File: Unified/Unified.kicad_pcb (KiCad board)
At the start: 2 copper layers, 72.4 x 72.4 mm, 56 parts, among them J1 USB_C_Receptacle_USB2.0_16P, J10 JST_switch_1, J11 JST_switch_2, J12 Conn_touch_1, J13 Conn_touch_2, J14 Bat_pos_sel, J15 Bat_neg_sel, J16 JST_header, J2 JST_battery, J3 JST_header, J4 JST_speaker, J5 JST_debug_swd, J6 JST_debug_serial, J7 Conn_speaker_sd, J8 Conn_speaker_gain, J9 Conn_speaker_gnd, Q1 AO3401A, Q2 AO3400A, SW1 SW_power, U1 MCP73831-2-OT, U2 MAX98357A

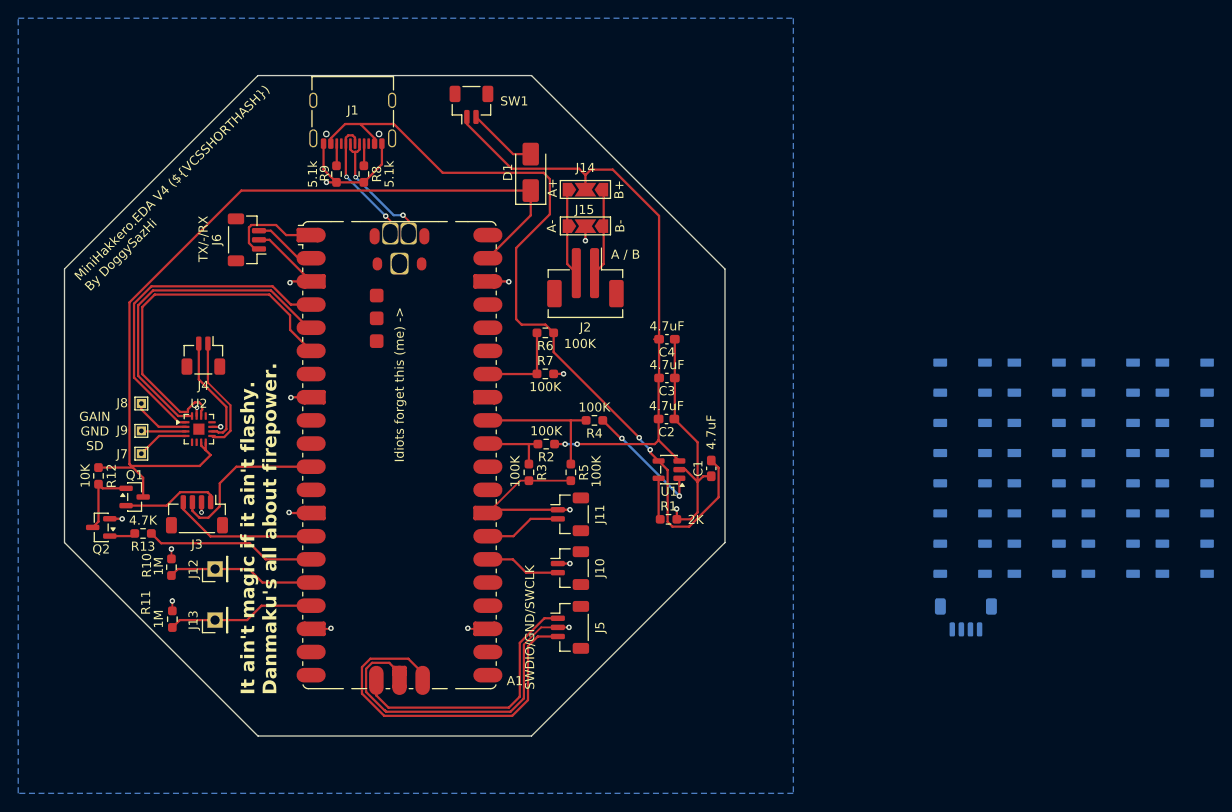
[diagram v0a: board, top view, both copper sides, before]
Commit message: Add LEDs to unified PCB, currently routing
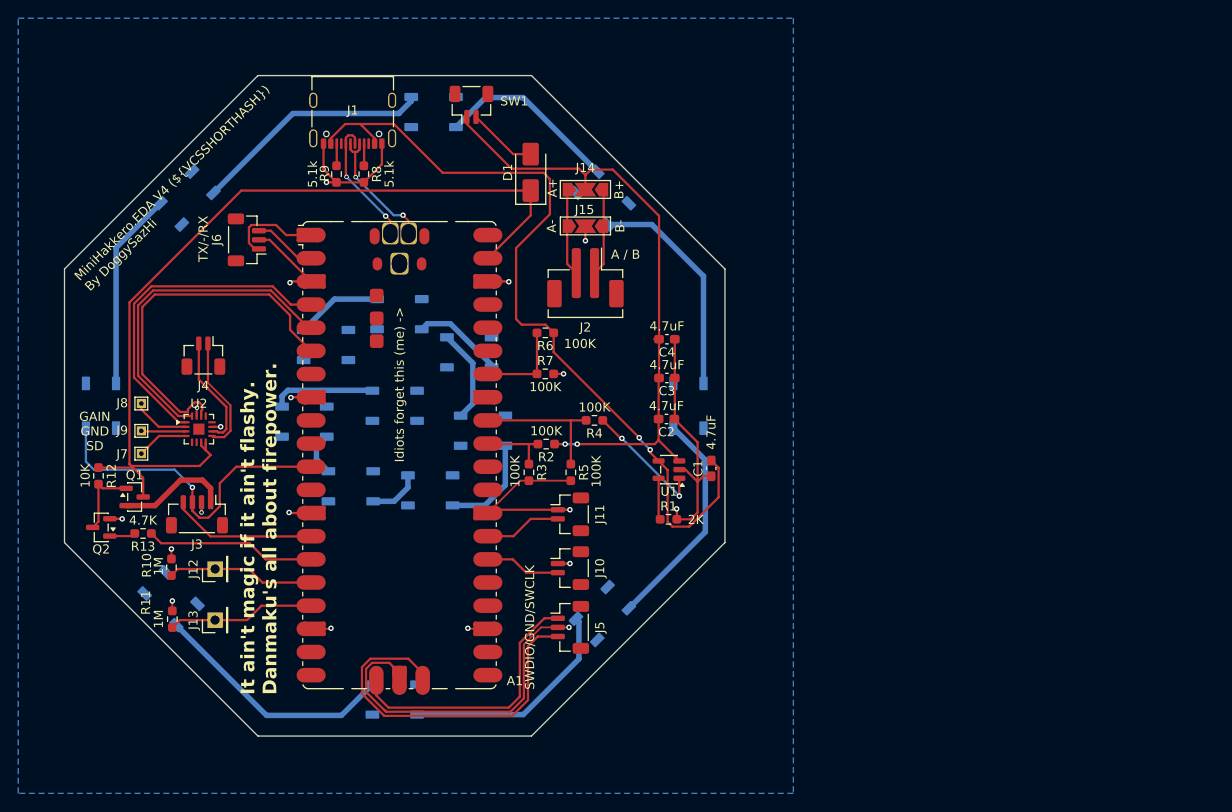
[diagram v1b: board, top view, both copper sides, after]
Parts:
- removed J16: JST_header, Connector_JST:JST_SH_BM04B-SRSS-TB_1x04-1MP_P1.00mm_Vertical
- moved D9 111.7 mm to (131.8, 123.7), turned to -45 degrees
- moved D16 96.6 mm to (146.4, 104.2), turned to 0 degrees
- moved D2 94.5 mm to (124.1, 102.5), turned to -90 degrees
- moved D15 92.2 mm to (151.5, 111.3), turned to 0 degrees
- moved D3 89.0 mm to (133.5, 79.7), turned to -135 degrees
- moved D17 88.2 mm to (156.3, 102.5)
- moved D10 81.4 mm to (148.8, 95.8), turned to 0 degrees
- moved D11 78.3 mm to (156.8, 92.5)
- moved D14 75.0 mm to (160.2, 111.8), turned to 0 degrees
- moved D8 73.8 mm to (156.3, 134.7), turned to 0 degrees
- moved D4 71.8 mm to (160.6, 70.3)
- moved D12 71.0 mm to (164.5, 96.6), turned to 0 degrees
- moved D13 69.2 mm to (166.0, 105.2)
- moved D5 55.9 mm to (179.1, 79.7), turned to 135 degrees
- moved D7 51.4 mm to (179.1, 125.3), turned to 45 degrees
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- renumbered D9 to D10, D10 to D11, D11 to D12, D12 to D13, D13 to D14, D14 to D15, D15 to D16, D16 to D9
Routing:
- net Net-(D8-DOUT): track 0.00 -> 27.0 mm
- net Net-(D3-DOUT): track 0.00 -> 26.3 mm
- net Net-(D7-DOUT): track 0.00 -> 24.8 mm
- net Net-(D6-DOUT): track 0.00 -> 24.7 mm
- net Net-(D5-DOUT): track 0.00 -> 24.6 mm
- net Net-(D2-DOUT): track 0.00 -> 21.8 mm
- net Net-(D4-DOUT): track 0.00 -> 20.2 mm
- net /WS2812B_DIN: track 18.1 -> 36.2 mm, vias 0 -> 1
- net Net-(D16-DOUT): track 0.00 -> 11.3 mm
- net Net-(D13-DOUT): track 0.00 -> 11.0 mm
- net Net-(D12-DOUT): track 0.00 -> 10.3 mm
- net Net-(D11-DOUT): track 0.00 -> 10.1 mm
- net Net-(D10-DOUT): track 0.00 -> 9.45 mm
- net Net-(D14-DOUT): track 0.00 -> 5.79 mm
- net Net-(D15-DOUT): track 0.00 -> 4.81 mm
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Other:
- board text added: "The present is me, da ze~"

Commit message: Try to route but Kicad decided to crash
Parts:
- moved D7 0.35 mm to (179.3, 125.0)
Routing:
- net /WS2812B_VS: track 12.3 -> 343.4 mm, vias 0 -> 1
- net Net-(D10-DIN): track 0.00 -> 36.5 mm, vias 0 -> 2

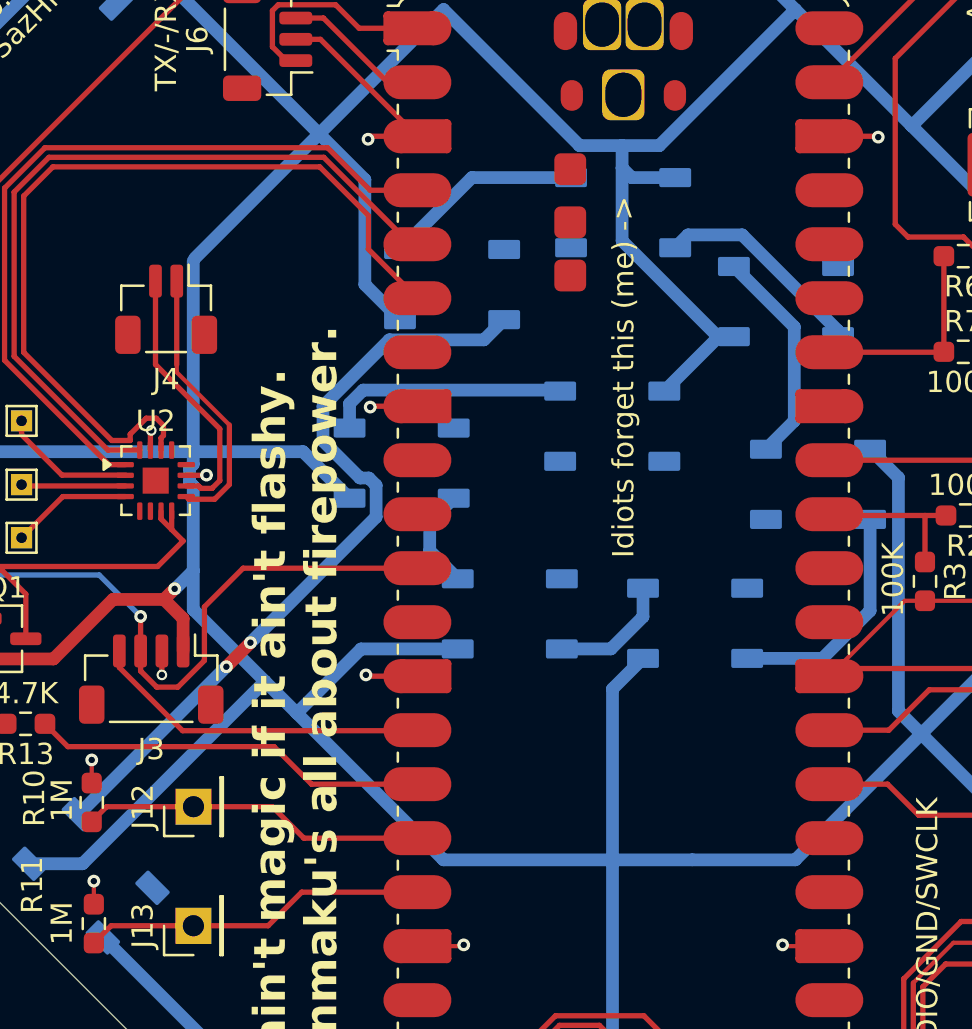
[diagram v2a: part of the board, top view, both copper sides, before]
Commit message: Finish main routing, plan to add other pinouts/mounting
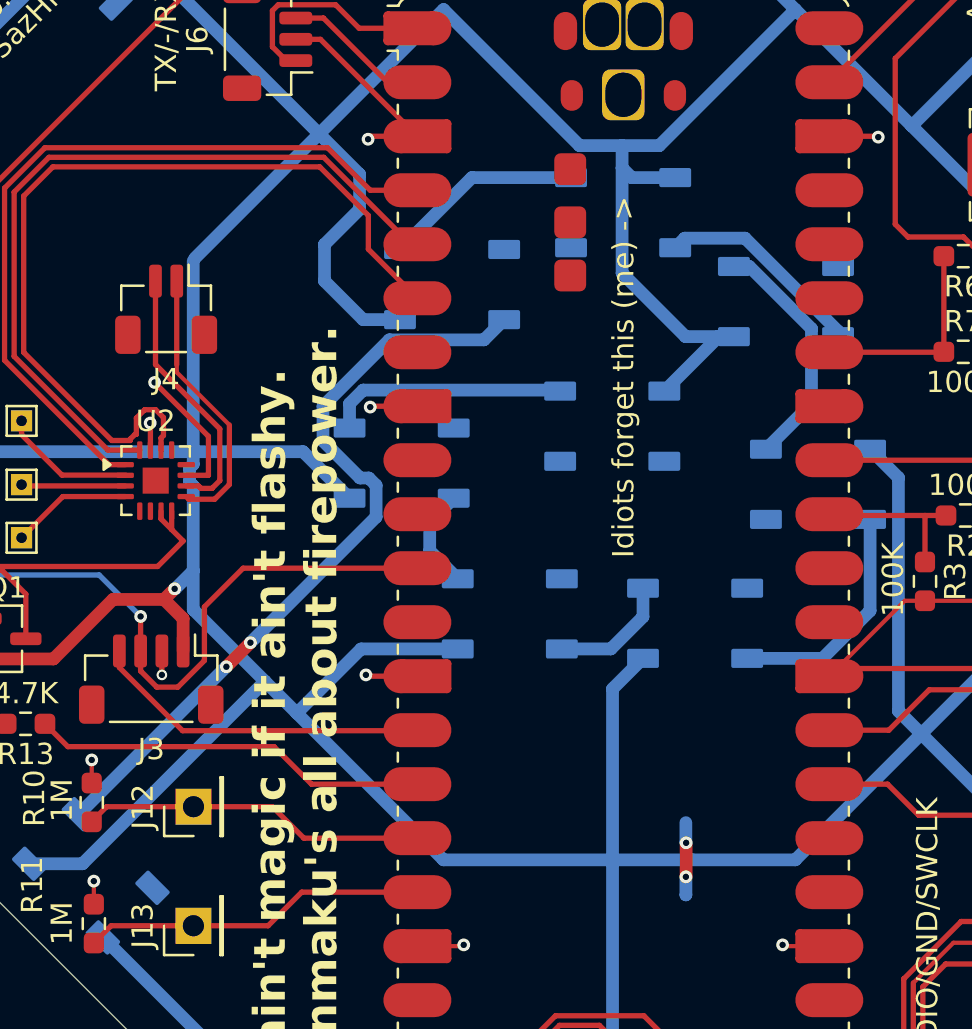
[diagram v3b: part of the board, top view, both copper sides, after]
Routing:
- net GND: track 136.1 -> 145.4 mm, vias 19 -> 21
- net /WS2812B_VS: track 343.4 -> 346.6 mm
- net Net-(D12-DOUT): track 10.3 -> 11.4 mm
- net /SPEAKER_LRC: track 40.2 -> 41.0 mm

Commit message: Re-arrange for pin header for speaker
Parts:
- added H1: MountingHole_Pad, MountingHole:MountingHole_2.2mm_M2_ISO7380_Pad, F.Cu at (183.0, 118.5)
- added H2: MountingHole_Pad, MountingHole:MountingHole_2.2mm_M2_ISO7380_Pad, F.Cu at (144.0, 76.0)
- added J16: Conn_01x02, Connector_PinHeader_2.54mm:PinHeader_1x02_P2.54mm_Vertical, F.Cu at (137.0, 92.5)
- added J17: Conn_01x07, Connector_PinSocket_2.54mm:PinSocket_1x07_P2.54mm_Vertical, F.Cu at (141.0, 109.1)
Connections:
- net Net-(J7-Pin_1) renamed /SPEAKER_SD
- net Net-(J8-Pin_1) renamed /SPEAKER_GAIN

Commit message: Finalize routing, bump to V5
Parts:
- moved J16 1.20 mm to (135.8, 92.5)
- moved H2 1.12 mm to (143.0, 76.5)
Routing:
- net /SW_+: track 96.1 -> 138.9 mm
- net /SPEAKER_SDA: track 36.8 -> 75.5 mm
- net /SPEAKER_SCL: track 36.8 -> 71.5 mm
- net /SPEAKER_LRC: track 41.0 -> 61.3 mm
- net /SPEAKER_-: track 12.4 -> 16.2 mm
- net /SPEAKER_+: track 13.0 -> 16.1 mm
- net GND: track 145.4 -> 147.7 mm, vias 21 -> 23
- net /WS2812B_VS: track 346.6 -> 348.7 mm
- net Net-(D10-DIN): track 36.5 -> 34.6 mm
- net /WS2812B_DIN: track 36.2 -> 34.7 mm

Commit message: Add 100k resistor for defaulting audio chip gain to 15dB
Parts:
- removed J7: Conn_speaker_sd, TestPoint:TestPoint_THTPad_1.0x1.0mm_Drill0.5mm
- removed J8: Conn_speaker_gain, TestPoint:TestPoint_THTPad_1.0x1.0mm_Drill0.5mm
- removed J9: Conn_speaker_gnd, TestPoint:TestPoint_THTPad_1.0x1.0mm_Drill0.5mm
- added R14: 100k, Resistor_SMD:R_0603_1608Metric_Pad0.98x0.95mm_HandSolder, F.Cu at (129.3, 104.8)
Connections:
- U2 pad 4: /SPEAKER_SD -> unconnected-(U2-~{SD_MODE}-Pad4)
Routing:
- net /SPEAKER_SD: track 5.68 -> 0.00 mm
- net /SPEAKER_GAIN: track 6.37 -> 3.18 mm
- net GND: track 147.7 -> 145.3 mm, vias 23 -> 25

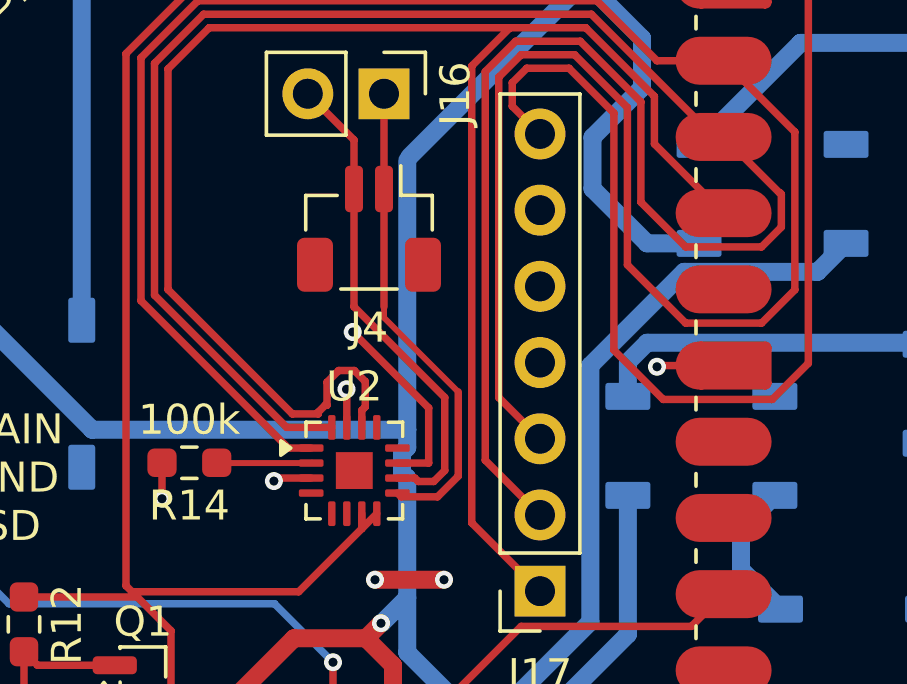
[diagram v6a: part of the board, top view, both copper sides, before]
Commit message: Add ground connection for MAX98357 pad, rewire GAIN and SD pins for header breakout, curse all actual EE nerds
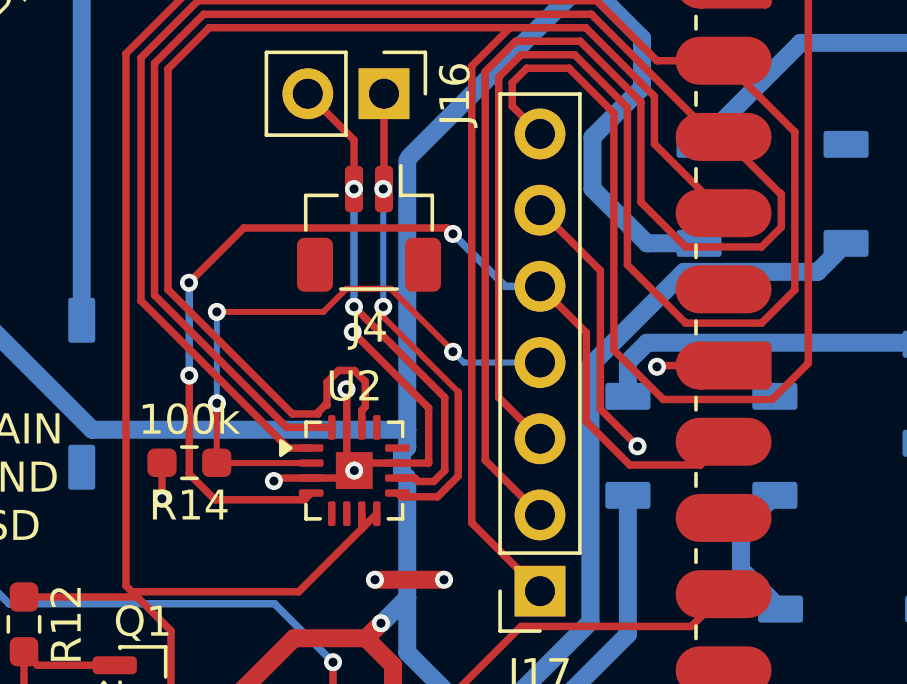
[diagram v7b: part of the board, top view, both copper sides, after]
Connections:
- A1 pad 9: unconnected-(A1-GPIO6-Pad9) -> /SPEAKER_SD
- J17 pad 4: unconnected-(J17-Pin_4-Pad4) -> /SPEAKER_GAIN
- J17 pad 5: unconnected-(J17-Pin_5-Pad5) -> /SPEAKER_SD
- U2 pad 17: unconnected-(U2-PAD-Pad17) -> GND
- U2 pad 4: unconnected-(U2-~{SD_MODE}-Pad4) -> /SPEAKER_SD
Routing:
- net /SPEAKER_SD: track 0.00 -> 34.8 mm, vias 0 -> 3
- net /SPEAKER_GAIN: track 3.18 -> 20.3 mm, vias 0 -> 3
- net GND: track 145.3 -> 159.1 mm, vias 25 -> 27
- net /SPEAKER_-: track 16.2 -> 16.3 mm, vias 0 -> 2
- net /SPEAKER_+: track 16.1 -> 16.2 mm, vias 0 -> 2
